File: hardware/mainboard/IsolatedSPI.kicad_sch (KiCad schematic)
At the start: 18 parts, among them IC3 BQ79600PWRQ1, IC6 LTC6820IMS

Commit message: sync
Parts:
- removed C18, C42: 100nF, Capacitor_SMD:C_0603_1608Metric, symbol Device:C_Small
- removed IC6: LTC6820IMS, Package_SO:MSOP-16_3x4.039mm_P0.5mm, symbol Samacsys_kicad_sym:LTC6820IMS
- removed R16, R19: 1k, Resistor_SMD:R_0603_1608Metric, symbol Device:R_Small
- removed R20: 120, Resistor_SMD:R_0603_1608Metric, symbol Device:R_Small
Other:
- note removed: "ISO SPI INTERFACE"
- moved on the sheet: C43, C53, C78, C79, C80, IC3, R94, R95, R96, R97, R98, R99

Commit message: schematic?
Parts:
- removed R94: 10k, Resistor_SMD:R_0603_1608Metric, symbol Device:R_Small
- removed R95: 100k, Resistor_SMD:R_0603_1608Metric, symbol Device:R_Small
- C79, C80: value 100p -> 100pF
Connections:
- net SCK is gone; now on net GND: IC3.6 (SCLK)
- net SPI_RDY is gone; now on net GND: IC3.8 (SPI_RDY)
- net ~{CS} is gone; now on net GND: IC3.7 (NCS)
- net +3.3VISO renamed +3.3VIO
- net +5VISO renamed +5VIO
- net GNDISO renamed GND
- net MISO renamed TX
- net MOSI renamed RX
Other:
- moved on the sheet: C80, R96, R98

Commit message: sync
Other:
- moved on the sheet: R96, R98
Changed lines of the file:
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@@
 	(wire
 		(pts
-			(xy 153.67 95.25) (xy 175.26 95.25)
+			(xy 153.67 95.25) (xy 186.69 95.25)
 		)
 		(stroke
@@
 	(wire
 		(pts
-			(xy 180.34 97.79) (xy 182.88 97.79)
-		)
-		(stroke
-			(width 0)
-			(type default)
-		)
-	)
-	(wire
-		(pts
-			(xy 165.1 97.79) (xy 175.26 97.79)
+			(xy 191.77 97.79) (xy 196.85 97.79)
+		)
+		(stroke
+			(width 0)
+			(type default)
+		)
+	)
+	(wire
+		(pts
+			(xy 165.1 97.79) (xy 186.69 97.79)
 		)
 		(stroke
@@
 	(wire
 		(pts
-			(xy 180.34 95.25) (xy 182.88 95.25)
+			(xy 191.77 95.25) (xy 196.85 95.25)
 		)
 		(stroke
@@
 	(hierarchical_label "OUT+"
 		(shape bidirectional)
-		(at 182.88 95.25 0)
+		(at 196.85 95.25 0)
 		(effects
 			(font
@@
 	(hierarchical_label "OUT-"
 		(shape bidirectional)
-		(at 182.88 97.79 0)
+		(at 196.85 97.79 0)
 		(effects
 			(font
@@
 			)
 			(justify left)
+		)
+	)
+	(netclass_flag ""
+		(length 2.54)
+		(shape round)
+		(at 177.8 95.25 0)
+		(fields_autoplaced yes)
+		(effects
+			(font
+				(size 1.27 1.27)
+			)
+			(justify left bottom)
+		)
+		(property "Netclass" "120Ohm"
+			(at 178.4096 92.71 0)
+			(effects
+				(font
+					(size 1.27 1.27)
+				)
+				(justify left)
+			)
+		)
+		(property "Component Class" ""
+			(at -95.25 2.54 0)
+			(effects
+				(font
+					(size 1.27 1.27)
+					(italic yes)
+				)
+				(justify right)
+			)
+		)
+	)
+	(netclass_flag ""
+		(length 2.54)
+		(shape round)
+		(at 177.8 97.79 180)
+		(fields_autoplaced yes)
+		(effects
+			(font
+				(size 1.27 1.27)
+			)
+			(justify right bottom)
+		)
+		(property "Netclass" "120Ohm"
+			(at 178.4096 100.33 0)
+			(effects
+				(font
+					(size 1.27 1.27)
+				)
+				(justify left)
+			)
+		)
+		(property "Component Class" ""
+			(at -95.25 190.5 0)
+			(effects
+				(font
+					(size 1.27 1.27)
+					(italic yes)
+				)
+				(justify right)
+			)
+		)
+	)
+	(netclass_flag ""
+		(length 2.54)
+		(shape round)
+		(at 194.31 95.25 0)
+		(fields_autoplaced yes)
+		(effects
+			(font
+				(size 1.27 1.27)
+			)
+			(justify left bottom)
+		)
+		(property "Netclass" "120Ohm"
+			(at 194.9196 92.71 0)
+			(effects
+				(font
+					(size 1.27 1.27)
+				)
+				(justify left)
+			)
+		)
+		(property "Component Class" ""
+			(at -78.74 2.54 0)
+			(effects
+				(font
+					(size 1.27 1.27)
+					(italic yes)
+				)
+				(justify right)
+			)
+		)
+	)
+	(netclass_flag ""
+		(length 2.54)
+		(shape round)
+		(at 194.31 97.79 180)
+		(fields_autoplaced yes)
+		(effects
+			(font
+				(size 1.27 1.27)
+			)
+			(justify right bottom)
+		)
+		(property "Netclass" "120Ohm"
+			(at 194.9196 100.33 0)
+			(effects
+				(font
+					(size 1.27 1.27)
+				)
+				(justify left)
+			)
+		)
+		(property "Component Class" ""
+			(at -78.74 190.5 0)
+			(effects
+				(font
+					(size 1.27 1.27)
+					(italic yes)
+				)
+				(justify right)
+			)
 		)
 	)
@@
 	(symbol
 		(lib_id "Device:R_Small")
-		(at 177.8 95.25 270)
+		(at 189.23 95.25 270)
 		(unit 1)
 		(exclude_from_sim no)
@@
 		(dnp no)
 		(property "Reference" "R96"
-			(at 177.8 90.17 90)
+			(at 189.23 90.17 90)
 			(effects
 				(font
@@
 		)
 		(property "Value" "51"
-			(at 177.8 92.71 90)
+			(at 189.23 92.71 90)
 			(effects
 				(font
@@
 		)
 		(property "Footprint" "Resistor_SMD:R_0603_1608Metric"
-			(at 177.8 95.25 0)
+			(at 189.23 95.25 0)
 			(effects
 				(font
@@
 		)
 		(property "Datasheet" "~"
-			(at 177.8 95.25 0)
+			(at 189.23 95.25 0)
 			(effects
 				(font
@@
 		)
 		(property "Description" ""
-			(at 177.8 95.25 0)
+			(at 189.23 95.25 0)
 			(effects
 				(font
@@
 		)
 		(property "Manufacturer_Name" "--"
-			(at 177.8 95.25 0)
+			(at 189.23 95.25 0)
 			(effects
 				(font
@@
 		)
 		(property "Manufacturer_Part_Number" "--"
-			(at 177.8 95.25 0)
+			(at 189.23 95.25 0)
 			(effects
 				(font
@@
 		)
 		(property "Arrow Part Number" ""
-			(at 177.8 95.25 0)
+			(at 189.23 95.25 0)
 			(effects
 				(font
@@
 		)
 		(property "Arrow Price/Stock" ""
-			(at 177.8 95.25 0)
+			(at 189.23 95.25 0)
 			(effects
 				(font
@@
 		)
 		(property "Mouser Part Number" "594-MCT06030C5109FP5"
-			(at 177.8 95.25 0)
+			(at 189.23 95.25 0)
 			(effects
 				(font
@@
 		)
 		(property "DigiKey Part Number" ""
-			(at 177.8 95.25 0)
+			(at 189.23 95.25 0)
 			(effects
 				(font
@@
 	(symbol
 		(lib_id "Device:R_Small")
-		(at 177.8 97.79 270)
+		(at 189.23 97.79 270)
 		(unit 1)
 		(exclude_from_sim no)
@@
 		(dnp no)
 		(property "Reference" "R98"
-			(at 177.8 100.33 90)
+			(at 189.23 100.33 90)
 			(effects
 				(font
@@
 		)
 		(property "Value" "51"
-			(at 177.8 102.87 90)
+			(at 189.23 102.87 90)
 			(effects
 				(font
@@
 		)
 		(property "Footprint" "Resistor_SMD:R_0603_1608Metric"
-			(at 177.8 97.79 0)
+			(at 189.23 97.79 0)
 			(effects
 				(font
@@
 		)
 		(property "Datasheet" "~"
-			(at 177.8 97.79 0)
+			(at 189.23 97.79 0)
 			(effects
 				(font
@@
 		)
 		(property "Description" ""
-			(at 177.8 97.79 0)
+			(at 189.23 97.79 0)
 			(effects
 				(font
@@
 		)
 		(property "Manufacturer_Name" "--"
-			(at 177.8 97.79 0)
+			(at 189.23 97.79 0)
 			(effects
 				(font
@@
 		)
 		(property "Manufacturer_Part_Number" "--"
-			(at 177.8 97.79 0)
+			(at 189.23 97.79 0)
 			(effects
 				(font
@@
 		)
 		(property "Arrow Part Number" ""
-			(at 177.8 97.79 0)
+			(at 189.23 97.79 0)
 			(effects
 				(font
@@
 		)
 		(property "Arrow Price/Stock" ""
-			(at 177.8 97.79 0)
+			(at 189.23 97.79 0)
 			(effects
 				(font
@@
 		)
 		(property "Mouser Part Number" "594-MCT06030C5109FP5"
-			(at 177.8 97.79 0)
+			(at 189.23 97.79 0)
 			(effects
 				(font
@@
 		)
 		(property "DigiKey Part Number" ""
-			(at 177.8 97.79 0)
-			(effects
-				(font
+			(at 189.23 97.79 0)
+			(effects
+				(font

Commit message: Layout again
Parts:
- added TP17, TP18: TestPoint_Small, TestPoint:TestPoint_Pad_D1.0mm, symbol Connector:TestPoint_Small
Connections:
- net COM+: now also TP17.1
- net COM-: now also TP18.1
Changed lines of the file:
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@@
+	)
+	(junction
+		(at 170.18 95.25)
+		(diameter 0)
+		(color 0 0 0 0)
+	)
+	(junction
+		(at 170.18 97.79)
+		(diameter 0)
+		(color 0 0 0 0)
 	)
 	(junction
@@
 	(wire
 		(pts
+			(xy 170.18 97.79) (xy 186.69 97.79)
+		)
+		(stroke
+			(width 0)
+			(type default)
+		)
+	)
+	(wire
+		(pts
 			(xy 140.97 92.71) (xy 140.97 97.79)
 		)
@@
 	(wire
 		(pts
-			(xy 153.67 95.25) (xy 186.69 95.25)
+			(xy 153.67 95.25) (xy 170.18 95.25)
 		)
 		(stroke
@@
 	(wire
 		(pts
+			(xy 170.18 92.71) (xy 170.18 95.25)
+		)
+		(stroke
+			(width 0)
+			(type default)
+		)
+	)
+	(wire
+		(pts
 			(xy 113.03 100.33) (xy 113.03 102.87)
 		)
@@
 	(wire
 		(pts
+			(xy 170.18 97.79) (xy 170.18 100.33)
+		)
+		(stroke
+			(width 0)
+			(type default)
+		)
+	)
+	(wire
+		(pts
 			(xy 113.03 102.87) (xy 115.57 102.87)
 		)
@@
 	(wire
 		(pts
-			(xy 165.1 97.79) (xy 186.69 97.79)
+			(xy 165.1 97.79) (xy 170.18 97.79)
 		)
 		(stroke
@@
 		(pts
 			(xy 179.07 62.23) (xy 179.07 59.69)
+		)
+		(stroke
+			(width 0)
+			(type default)
+		)
+	)
+	(wire
+		(pts
+			(xy 170.18 95.25) (xy 186.69 95.25)
 		)
 		(stroke
@@
 		(dnp no)
 		(property "Reference" "C79"
-			(at 156.21 101.6 0)
+			(at 145.288 101.854 0)
 			(show_name no)
 			(do_not_autoplace no)
@@
 		)
 		(property "Value" "100pF"
-			(at 156.21 104.14 0)
+			(at 145.288 104.394 0)
 			(show_name no)
 			(do_not_autoplace no)
@@
 				(path "/b456cffc-d9d7-4c91-91f2-36ec9a65dd1b/6b45fd0b-238d-49b3-829e-372c6baba47f"
 					(reference "C79")
+					(unit 1)
+				)
+			)
+		)
+	)
+	(symbol
+		(lib_id "Connector:TestPoint_Small")
+		(at 170.18 92.71 0)
+		(unit 1)
+		(body_style 1)
+		(exclude_from_sim no)
+		(in_bom yes)
+		(on_board yes)
+		(in_pos_files yes)
+		(dnp no)
+		(property "Reference" "TP17"
+			(at 161.544 88.392 0)
+			(show_name no)
+			(do_not_autoplace no)
+			(effects
+				(font
+					(size 1.27 1.27)
+				)
+				(justify left)
+			)
+		)
+		(property "Value" "TestPoint_Small"
+			(at 161.544 90.932 0)
+			(show_name no)
+			(do_not_autoplace no)
+			(effects
+				(font
+					(size 1.27 1.27)
+				)
+				(justify left)
+			)
+		)
+		(property "Footprint" "TestPoint:TestPoint_Pad_D1.0mm"
+			(at 175.26 92.71 0)
+			(hide yes)
+			(show_name no)
+			(do_not_autoplace no)
+			(effects
+				(font
+					(size 1.27 1.27)
+				)
+			)
+		)
+		(property "Datasheet" ""
+			(at 175.26 92.71 0)
+			(hide yes)
+			(show_name no)
+			(do_not_autoplace no)
+			(effects
+				(font
+					(size 1.27 1.27)
+				)
+			)
+		)
+		(property "Description" "test point"
+			(at 170.18 92.71 0)
+			(hide yes)
+			(show_name no)
+			(do_not_autoplace no)
+			(effects
+				(font
+					(size 1.27 1.27)
+				)
+			)
+		)
+		(pin "1"
+		)
+		(instances
+			(project "PUTM_EV_AMS_MASTER"
+				(path "/b456cffc-d9d7-4c91-91f2-36ec9a65dd1b/6b45fd0b-238d-49b3-829e-372c6baba47f"
+					(reference "TP17")
 					(unit 1)
 				)
@@
 		(dnp no)
 		(property "Reference" "C80"
-			(at 167.64 101.6 0)
+			(at 156.718 101.854 0)
 			(show_name no)
 			(do_not_autoplace no)
@@
 		)
 		(property "Value" "100pF"
-			(at 167.64 104.14 0)
+			(at 156.718 104.394 0)
 			(show_name no)
 			(do_not_autoplace no)
@@
 					(unit 1)
 				)
+			)
+		)
+	)
+	(symbol
+		(lib_id "Connector:TestPoint_Small")
+		(at 170.18 100.33 180)
+		(unit 1)
+		(body_style 1)
+		(exclude_from_sim no)
+		(in_bom yes)
+		(on_board yes)
+		(in_pos_files yes)
+		(dnp no)
+		(property "Reference" "TP18"
+			(at 172.974 105.156 0)
+			(show_name no)
+			(do_not_autoplace no)
+			(effects
+				(font
+					(size 1.27 1.27)
+				)
+				(justify left)
+			)
+		)
+		(property "Value" "TestPoint_Small"
+			(at 183.642 102.87 0)
+			(show_name no)
+			(do_not_autoplace no)
+			(effects
+				(font
+					(size 1.27 1.27)
+				)
+				(justify left)
+			)
+		)
+		(property "Footprint" "TestPoint:TestPoint_Pad_D1.0mm"
+			(at 165.1 100.33 0)
+			(hide yes)
+			(show_name no)
+			(do_not_autoplace no)
+			(effects
+				(font
+					(size 1.27 1.27)
+				)
+			)
+		)
+		(property "Datasheet" ""
+			(at 165.1 100.33 0)
+			(hide yes)
+			(show_name no)
+			(do_not_autoplace no)
+			(effects
+				(font
+					(size 1.27 1.27)
+				)
+			)
+		)
+		(property "Description" "test point"
+			(at 170.18 100.33 0)
+			(hide yes)
+			(show_name no)
+			(do_not_autoplace no)
+			(effects
+				(font
+					(size 1.27 1.27)
+				)
+			)
+		)
+		(pin "1"
+		)
+		(instances
+			(project "PUTM_EV_AMS_MASTER"
+				(path "/b456cffc-d9d7-4c91-91f2-36ec9a65dd1b/6b45fd0b-238d-49b3-829e-372c6baba47f"
+					(reference "TP18")
+					(unit 1)
+				)

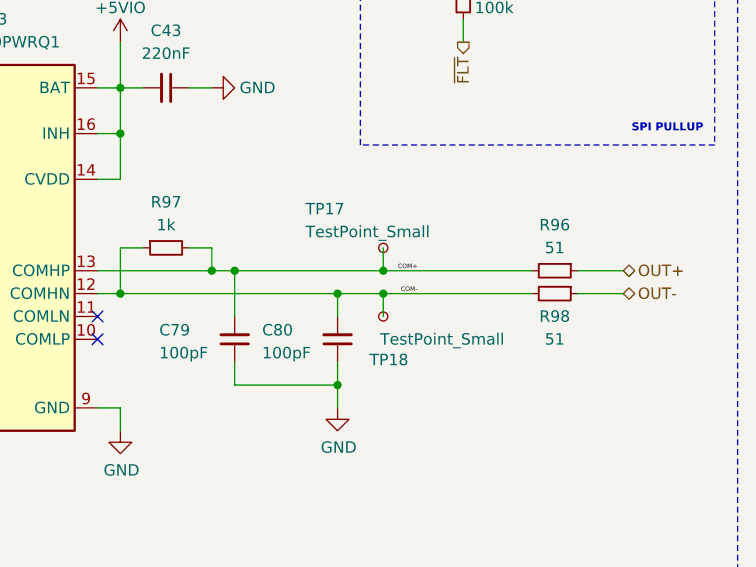
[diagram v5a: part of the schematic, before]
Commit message: Plytka chyba fajnie zrobiona oprocz teardropow bo kicad 10 jest dziwny
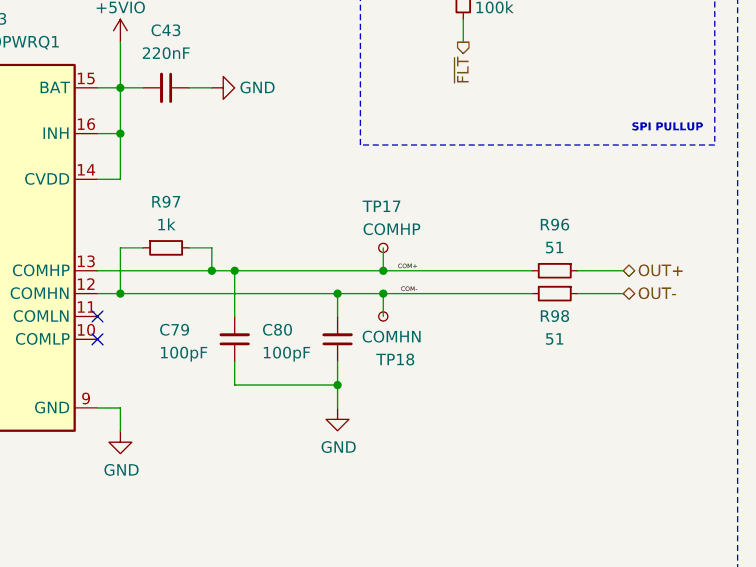
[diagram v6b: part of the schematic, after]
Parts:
- TP17: value TestPoint_Small -> COMHP
- TP18: value TestPoint_Small -> COMHN
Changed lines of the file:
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@@
 		(dnp no)
 		(property "Reference" "TP17"
-			(at 161.544 88.392 0)
+			(at 167.894 88.138 0)
 			(show_name no)
 			(do_not_autoplace no)
@@
 			)
 		)
-		(property "Value" "TestPoint_Small"
-			(at 161.544 90.932 0)
+		(property "Value" "COMHP"
+			(at 167.894 90.678 0)
 			(show_name no)
 			(do_not_autoplace no)
@@
 		(dnp no)
 		(property "Reference" "TP18"
-			(at 172.974 105.156 0)
+			(at 173.736 105.156 0)
 			(show_name no)
 			(do_not_autoplace no)
@@
 			)
 		)
-		(property "Value" "TestPoint_Small"
-			(at 183.642 102.87 0)
-			(show_name no)
-			(do_not_autoplace no)
+		(property "Value" "COMHN"
+			(at 174.498 102.616 0)
+			(show_name no)
+			(do_not_autoplace no)

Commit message: sync
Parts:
- removed TP17: COMHP, TestPoint:TestPoint_Pad_D1.0mm, symbol Connector:TestPoint_Small
- removed TP18: COMHN, TestPoint:TestPoint_Pad_D1.0mm, symbol Connector:TestPoint_Small
